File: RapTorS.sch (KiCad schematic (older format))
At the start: 22 parts, among them J1 USB_A, J2 TestPoint, J3 TestPoint, J4 TestPoint, J5 TestPoint, J6 TestPoint, U1 PIC16LF1454-I_ML, U2 TLV71333PDBV, U3 E07-M1101S

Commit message: every values OK
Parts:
- D1, D2: footprint (none) -> LEDs:LED_0805
- R2, R3: value R -> 50R; footprint (none) -> Resistors_SMD:R_0805
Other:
- note removed: "=== TODO ===\nsuivre toutes les recommandations USB de la note d’application\n"
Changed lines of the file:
@@
 U 1 1 5B61E4BB
 P 1550 5550
-F 0 "D1" H 1500 5300 50  0000 C CNN
-F 1 "LED_ALT" H 1600 5400 50  0000 C CNN
-F 2 "" H 1550 5550 50  0001 C CNN
+F 0 "D1" H 1550 5400 50  0000 C CNN
+F 1 "LED_ALT" H 1600 5400 50  0001 C CNN
+F 2 "LEDs:LED_0805" H 1550 5550 50  0001 C CNN
 F 3 "~" H 1550 5550 50  0001 C CNN
 	1    1550 5550
@@
 Text GLabel 6100 2200 0    50   Input ~ 0
 ~MCLR
-Text Notes 600  7250 0    50   ~ 0
-=== TODO ===\nsuivre toutes les recommandations USB de la note d’application\n
 Text GLabel 9650 1400 2    50   BiDi ~ 0
 ISPDAT
@@
 P 1550 5150
 F 0 "R2" H 1620 5196 50  0000 L CNN
-F 1 "R" H 1620 5105 50  0000 L CNN
-F 2 "" V 1480 5150 50  0001 C CNN
+F 1 "50R" H 1620 5105 50  0000 L CNN
+F 2 "Resistors_SMD:R_0805" V 1480 5150 50  0001 C CNN
 F 3 "" H 1550 5150 50  0001 C CNN
 	1    1550 5150
@@
 U 1 1 5B7DCADD
 P 2450 5550
-F 0 "D2" H 2400 5300 50  0000 C CNN
-F 1 "LED_ALT" H 2500 5400 50  0000 C CNN
-F 2 "" H 2450 5550 50  0001 C CNN
+F 0 "D2" H 2450 5400 50  0000 C CNN
+F 1 "LED_ALT" H 2500 5400 50  0001 C CNN
+F 2 "LEDs:LED_0805" H 2450 5550 50  0001 C CNN
 F 3 "~" H 2450 5550 50  0001 C CNN
 	1    2450 5550
@@
 P 2450 5150
 F 0 "R3" H 2520 5196 50  0000 L CNN
-F 1 "R" H 2520 5105 50  0000 L CNN
-F 2 "" V 2380 5150 50  0001 C CNN
+F 1 "50R" H 2520 5105 50  0000 L CNN
+F 2 "Resistors_SMD:R_0805" V 2380 5150 50  0001 C CNN
 F 3 "" H 2450 5150 50  0001 C CNN
 	1    2450 5150

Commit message: add E07 footprint, associate all footprints
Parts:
- ANT1: footprint (none) -> Connectors:Pin_d1.0mm_L10.0mm
- C1, C2: footprint (none) -> Capacitors_SMD:C_0805
- C3: footprint (none) -> Capacitors_SMD:CP_Elec_5x5.7
- J1: footprint (none) -> Capacitors_SMD:CP_Elec_4x4.5
- J2: footprint (none) -> Connectors_TestPoints:Test_Point_Pad_1.5x1.5mm
- J3, J4, J5, J6: footprint (none) -> Connectors_TestPoints:Test_Point_Pad_d1.5mm
- U1: footprint (none) -> Housings_DFN_QFN:QFN-16-1EP_4x4mm_Pitch0.65mm
- U3: footprint (none) -> E07-M1101S:E07-M1101S
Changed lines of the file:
@@
 F 0 "ANT1" H 9278 3290 50  0000 L CNN
 F 1 "antenna_433Mhz" H 9278 3199 50  0000 L CNN
-F 2 "" H 9050 3600 50  0001 C CNN
+F 2 "Connectors:Pin_d1.0mm_L10.0mm" H 9050 3600 50  0001 C CNN
 F 3 "" H 9050 3600 50  0001 C CNN
 	1    9050 3600
@@
 F 0 "J1" H 1405 1917 50  0000 C CNN
 F 1 "USB_A" H 1405 1826 50  0000 C CNN
-F 2 "" H 1500 1400 50  0001 C CNN
+F 2 "Capacitors_SMD:CP_Elec_4x4.5" H 1500 1400 50  0001 C CNN
 F 3 "" H 1500 1400 50  0001 C CNN
 	1    1350 1450
@@
 F 0 "C2" H 3015 1596 50  0000 L CNN
 F 1 "100nF" H 3015 1505 50  0000 L CNN
-F 2 "" H 2938 1400 50  0001 C CNN
+F 2 "Capacitors_SMD:C_0805" H 2938 1400 50  0001 C CNN
 F 3 "" H 2900 1550 50  0001 C CNN
 	1    2900 1550
@@
 F 0 "C1" H 2265 1596 50  0000 L CNN
 F 1 "10nF" H 2265 1505 50  0000 L CNN
-F 2 "" H 2188 1400 50  0001 C CNN
+F 2 "Capacitors_SMD:C_0805" H 2188 1400 50  0001 C CNN
 F 3 "" H 2150 1550 50  0001 C CNN
 	1    2150 1550
@@
 F 0 "C3" H 3435 1596 50  0000 R CNN
 F 1 "4.7uF" H 3435 1505 50  0000 R CNN
-F 2 "" H 3550 1550 50  0001 C CNN
+F 2 "Capacitors_SMD:CP_Elec_5x5.7" H 3550 1550 50  0001 C CNN
 F 3 "" H 3550 1550 50  0001 C CNN
 	1    3550 1550
@@
 F 0 "U3" H 8150 4275 50  0000 C CNN
 F 1 "E07-M1101S" H 8150 4184 50  0000 C CNN
-F 2 "" H 8150 4150 50  0001 C CNN
+F 2 "E07-M1101S:E07-M1101S" H 8150 4150 50  0001 C CNN
 F 3 "" H 8150 4150 50  0001 C CNN
 	1    8150 4150
@@
 F 0 "U1" H 9900 2450 50  0000 C CNN
 F 1 "PIC16LF1454-I_ML" H 9550 2350 50  0000 C CNN
-F 2 "" H 8150 1800 50  0001 C CNN
+F 2 "Housings_DFN_QFN:QFN-16-1EP_4x4mm_Pitch0.65mm" H 8150 1800 50  0001 C CNN
 F 3 "http://ww1.microchip.com/downloads/en/DeviceDoc/41639A.pdf" H 8150 1800 50  0001 C CNN
 	1    8150 1800
@@
 F 0 "J2" V 5700 3787 50  0000 L CNN
 F 1 "TestPoint" V 5745 3788 50  0001 L CNN
-F 2 "" H 5900 3600 50  0001 C CNN
+F 2 "Connectors_TestPoints:Test_Point_Pad_1.5x1.5mm" H 5900 3600 50  0001 C CNN
 F 3 "~" H 5900 3600 50  0001 C CNN
 	1    5700 3600
@@
 F 0 "J3" V 5700 3987 50  0000 L CNN
 F 1 "TestPoint" V 5745 3988 50  0001 L CNN
-F 2 "" H 5900 3800 50  0001 C CNN
+F 2 "Connectors_TestPoints:Test_Point_Pad_d1.5mm" H 5900 3800 50  0001 C CNN
 F 3 "~" H 5900 3800 50  0001 C CNN
 	1    5700 3800
@@
 F 0 "J4" V 5700 4187 50  0000 L CNN
 F 1 "TestPoint" V 5745 4188 50  0001 L CNN
-F 2 "" H 5900 4000 50  0001 C CNN
+F 2 "Connectors_TestPoints:Test_Point_Pad_d1.5mm" H 5900 4000 50  0001 C CNN
 F 3 "~" H 5900 4000 50  0001 C CNN
 	1    5700 4000
@@
 F 0 "J5" V 5700 4387 50  0000 L CNN
 F 1 "TestPoint" V 5745 4388 50  0001 L CNN
-F 2 "" H 5900 4200 50  0001 C CNN
+F 2 "Connectors_TestPoints:Test_Point_Pad_d1.5mm" H 5900 4200 50  0001 C CNN
 F 3 "~" H 5900 4200 50  0001 C CNN
 	1    5700 4200
@@
 F 0 "J6" V 5700 4587 50  0000 L CNN
 F 1 "TestPoint" V 5745 4588 50  0001 L CNN
-F 2 "" H 5900 4400 50  0001 C CNN
+F 2 "Connectors_TestPoints:Test_Point_Pad_d1.5mm" H 5900 4400 50  0001 C CNN
 F 3 "~" H 5900 4400 50  0001 C CNN
 	1    5700 4400

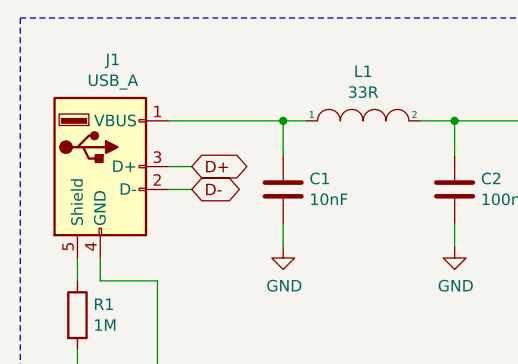
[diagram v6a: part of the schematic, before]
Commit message: update USB connector ref
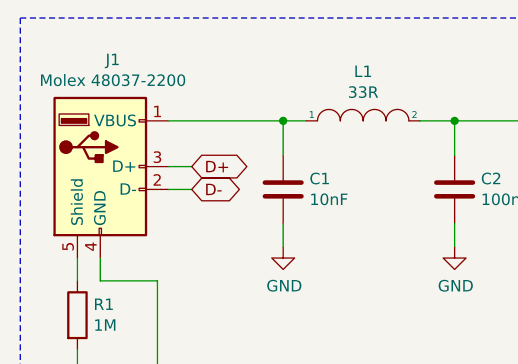
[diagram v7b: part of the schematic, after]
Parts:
- C3: footprint Capacitors_SMD:CP_Elec_5x5.7 -> Capacitors_SMD:CP_Elec_4x4.5
- J1: value USB_A -> Molex 48037-2200
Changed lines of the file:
@@
 P 1350 1450
 F 0 "J1" H 1405 1917 50  0000 C CNN
-F 1 "USB_A" H 1405 1826 50  0000 C CNN
+F 1 "Molex 48037-2200" H 1405 1826 50  0000 C CNN
 F 2 "Capacitors_SMD:CP_Elec_4x4.5" H 1500 1400 50  0001 C CNN
 F 3 "" H 1500 1400 50  0001 C CNN
@@
 F 0 "C3" H 3435 1596 50  0000 R CNN
 F 1 "4.7uF" H 3435 1505 50  0000 R CNN
-F 2 "Capacitors_SMD:CP_Elec_5x5.7" H 3550 1550 50  0001 C CNN
+F 2 "Capacitors_SMD:CP_Elec_4x4.5" H 3550 1550 50  0001 C CNN
 F 3 "" H 3550 1550 50  0001 C CNN
 	1    3550 1550

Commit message: finish USB footprint
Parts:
- J1: footprint Capacitors_SMD:CP_Elec_4x4.5 -> PX_Molex:MOLEX_USB_48037-2200
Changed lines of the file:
@@
 F 0 "J1" H 1405 1917 50  0000 C CNN
 F 1 "Molex 48037-2200" H 1405 1826 50  0000 C CNN
-F 2 "Capacitors_SMD:CP_Elec_4x4.5" H 1500 1400 50  0001 C CNN
+F 2 "PX_Molex:MOLEX_USB_48037-2200" H 1500 1400 50  0001 C CNN
 F 3 "" H 1500 1400 50  0001 C CNN
 	1    1350 1450
